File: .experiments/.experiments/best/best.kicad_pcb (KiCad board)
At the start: 2 copper layers, 140 x 90 mm, 39 parts, among them J1 USB_C, J2 Output, J3 Debug, Q1 FS8205A, U1 USBLC6-2SC6, U2 BQ24072, U3 HY2113-KB5B, U4 MT3608, U5 AP2112K-3.3, U6 LN61CN3302MR-G

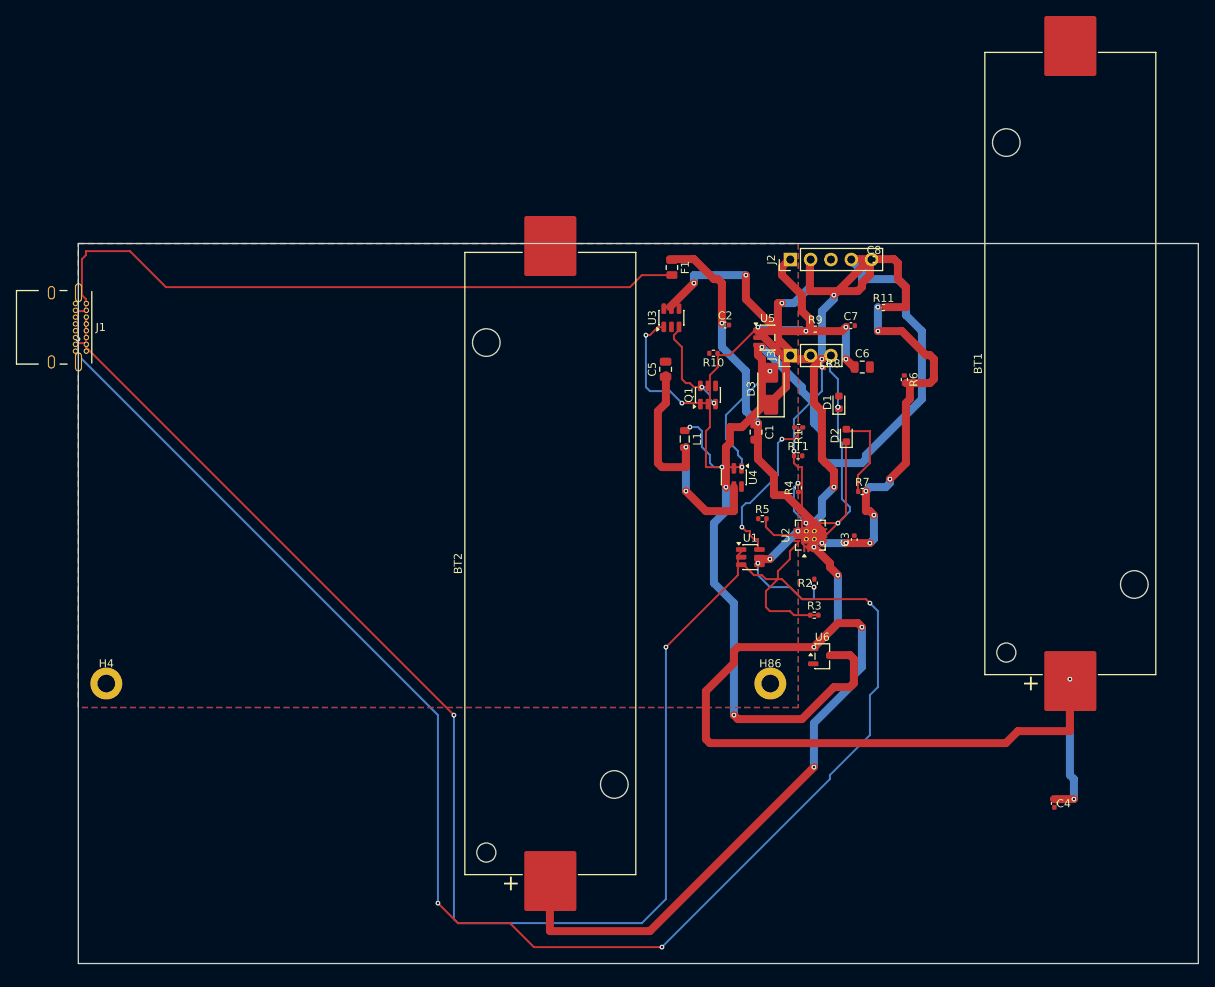
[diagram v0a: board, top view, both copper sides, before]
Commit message: Set uniform 6mil trace width (0.1524mm) for signal+power to reduce shorts
Baseline with 6mil: score=20.05 shorts=72 (vs 25.66@82shorts before)
Round 1: 20.45 shorts=93
Round 2: 20.65 shorts=84 [NEW BEST]
Round 3: 19.44 shorts=72

Trading off routing flexibility for cleaner DRC (no catastrophic shorts).
Tighter routing but more predictable.

Co-Authored-By: Claude Opus 4.6 <noreply@anthropic.com>
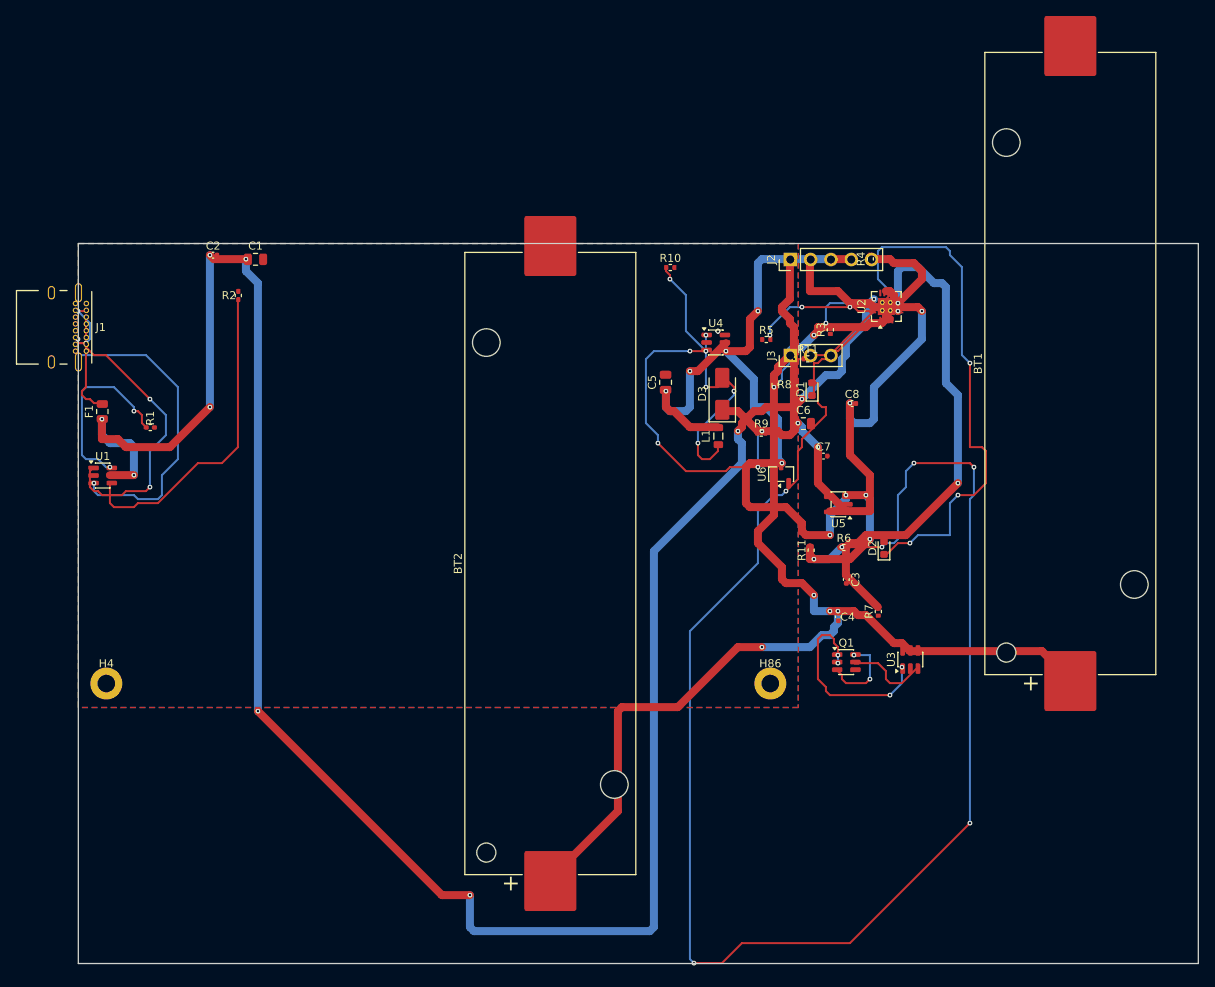
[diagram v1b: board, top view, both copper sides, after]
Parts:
- moved U1 81.6 mm to (3.04, 29.0)
- moved R1 81.0 mm to (9.00, 23.0), turned to 0 degrees
- moved R2 80.5 mm to (20.0, 6.50)
- moved F1 73.4 mm to (3.00, 21.0), turned to 90 degrees
- moved C1 66.2 mm to (22.1, 1.97), turned to 0 degrees
- moved C2 64.6 mm to (16.9, 1.46)
- moved U3 52.1 mm to (104.0, 52.0)
- moved Q1 37.6 mm to (96.0, 52.3), turned to 0 degrees
- moved R3 35.7 mm to (94.0, 10.8), turned to 90 degrees
- moved C4 35.7 mm to (95.0, 46.7)
- moved R11 31.7 mm to (91.6, 38.3), turned to 90 degrees
- moved U2 30.1 mm to (101.0, 7.87)
- moved R4 30.0 mm to (99.0, 1.92)
- moved U6 23.3 mm to (87.8, 28.8), turned to 90 degrees
- moved U5 22.6 mm to (95.0, 32.6), turned to 180 degrees
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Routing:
- net /VBUS: track 52.8 -> 269.7 mm, vias 4 -> 10
- net Net-(D1-A): track 0.00 -> 193.9 mm, vias 0 -> 6
- net Net-(J1-CC2): track 192.1 -> 40.6 mm, vias 4 -> 2
- net Net-(J1-CC1): track 169.9 -> 38.4 mm
- net /VBAT: track 253.3 -> 161.6 mm, vias 12 -> 6
- net Net-(F1-Pad2): track 89.4 -> 17.4 mm, vias 0 -> 2
- net /EN: track 146.3 -> 89.6 mm, vias 4 -> 8
- net Net-(D2-K): track 13.0 -> 67.3 mm, vias 0 -> 4
- net /3V3: track 26.4 -> 60.0 mm
- net Net-(R2-Pad1): track 11.2 -> 40.3 mm, vias 2 -> 0
- net /VSYS: track 51.9 -> 72.6 mm, vias 8 -> 6
- net Net-(U4-FB): track 31.3 -> 51.0 mm, vias 2 -> 6
- net Net-(D2-A): track 11.1 -> 0.00 mm
- net Net-(U2-TMR): track 5.41 -> 15.7 mm, vias 0 -> 2
- net /NTC_SENSE: track 27.0 -> 17.6 mm
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
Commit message: Hard-block cross-net traces to eliminate shorts (50% of DRC failures)
Critical fixes:
- Mark routed traces/vias at 1e6 (hard block) in solve() instead of 100 (soft)
- A* now cannot cross completed nets → no more shorting through existing traces
- Mark escape vias on grid immediately (was invisible, caused via collisions)
- Add clearance margin to via markings (0.5mm approach distance enforced)
- Raise max_search to 2M (hard blocks require longer detours)
- Wire max_search config through __init__ and all find_path calls

Test added: test_hard_block_prevents_cross_net_routing verifies blocked cells
are uncrossable, forcing detours instead.

Expected impact: DRC shorts should drop from ~80 to near-zero.

Co-Authored-By: Claude Opus 4.6 <noreply@anthropic.com>
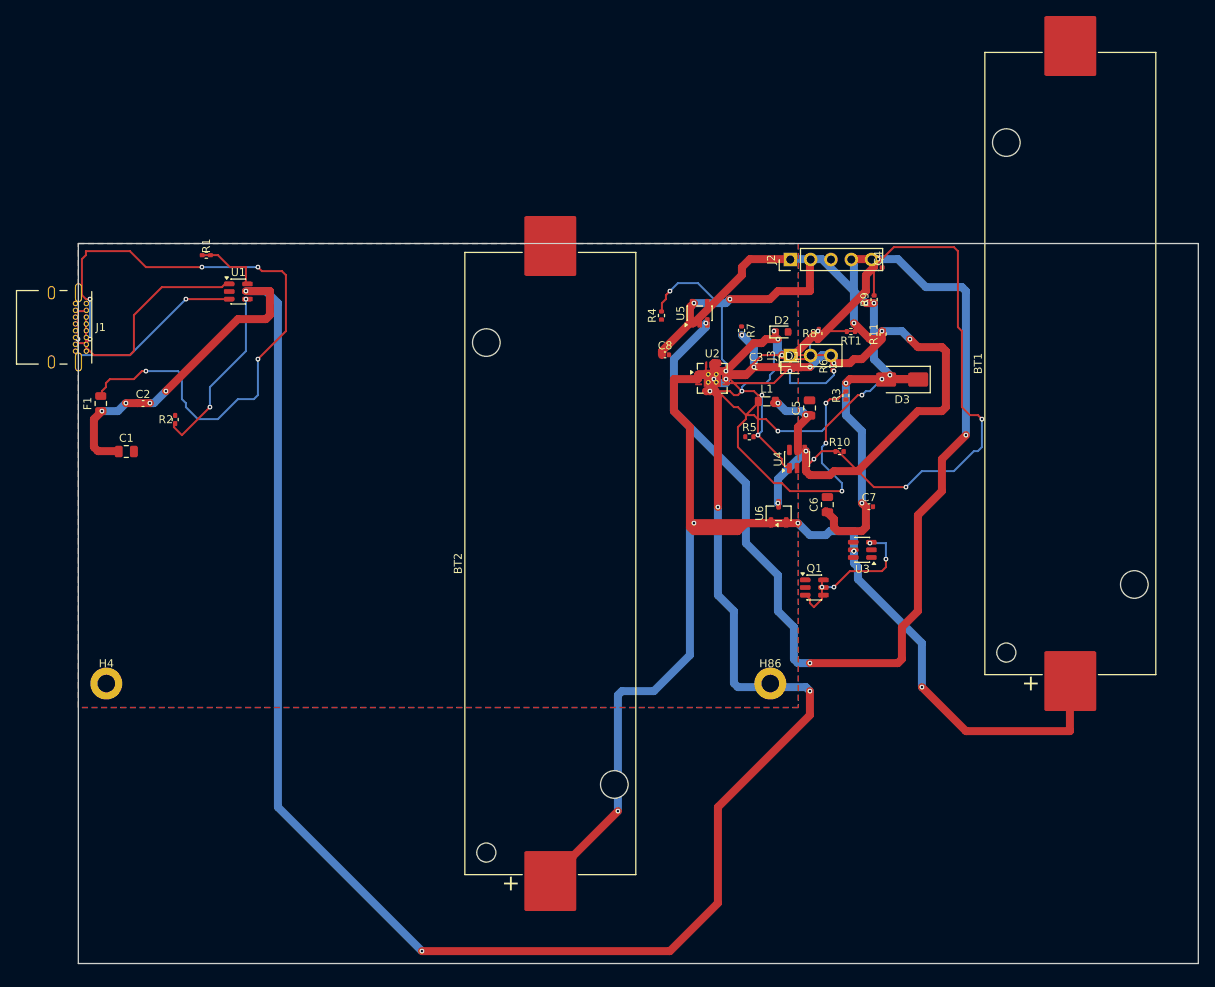
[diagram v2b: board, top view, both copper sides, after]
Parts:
- moved C4 44.0 mm to (100.0, 3.00), turned to 0 degrees
- moved R7 39.1 mm to (82.9, 10.9), turned to -90 degrees
- moved R10 31.3 mm to (95.2, 26.0)
- moved D2 29.9 mm to (87.9, 11.1), turned to 0 degrees
- moved U5 29.5 mm to (77.7, 8.72), turned to 90 degrees
- moved C1 28.9 mm to (6.00, 26.0)
- moved C3 28.9 mm to (84.7, 15.4), turned to 0 degrees
- moved U1 28.6 mm to (20.0, 6.00)
- moved R11 28.5 mm to (100.6, 11.3)
- moved R4 27.0 mm to (72.9, 9.00)
- moved C8 24.2 mm to (73.3, 13.9)
- moved U2 23.5 mm to (79.2, 16.8), turned to 0 degrees
- moved R6 22.7 mm to (94.3, 15.3), turned to 90 degrees
- moved R1 22.6 mm to (16.0, 1.47)
- moved D3 22.6 mm to (103.0, 17.0), turned to 180 degrees
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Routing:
- net Net-(D1-A): track 193.9 -> 9.12 mm, vias 6 -> 2
- net /EN: track 89.6 -> 190.2 mm, vias 8 -> 10
- net Net-(F1-Pad2): track 17.4 -> 88.4 mm, vias 2 -> 6
- net Net-(D2-K): track 67.3 -> 14.5 mm, vias 4 -> 2
- net /VSYS: track 72.6 -> 31.6 mm, vias 6 -> 7
- net /3V3: track 60.0 -> 27.3 mm
- net /VBAT: track 161.6 -> 192.1 mm, vias 6 -> 8
- net /5V: track 47.0 -> 77.3 mm, vias 2 -> 6
- net Net-(D3-A): track 25.6 -> 51.0 mm
- net Net-(Q1A-G): track 24.9 -> 0.00 mm, vias 4 -> 0
- net Net-(U2-ILIM): track 0.00 -> 19.3 mm, vias 0 -> 2
- net Net-(R2-Pad1): track 40.3 -> 22.2 mm, vias 0 -> 2
- net Net-(U4-FB): track 51.0 -> 68.3 mm, vias 6 -> 2
- net Net-(J1-CC2): track 40.6 -> 23.9 mm
- net Net-(U2-ISET): track 9.33 -> 26.0 mm
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
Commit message: Clean up: remove 50M+ of old experiment artifacts
Removed:
- .tmp_router_regression/ (11M baseline)
- .experiments/workers/ (40M+ old copies)
- .experiments/frames/ (old snapshots)

Kept: latest PCB, GIF, config, results

Co-Authored-By: Claude Opus 4.6 <noreply@anthropic.com>
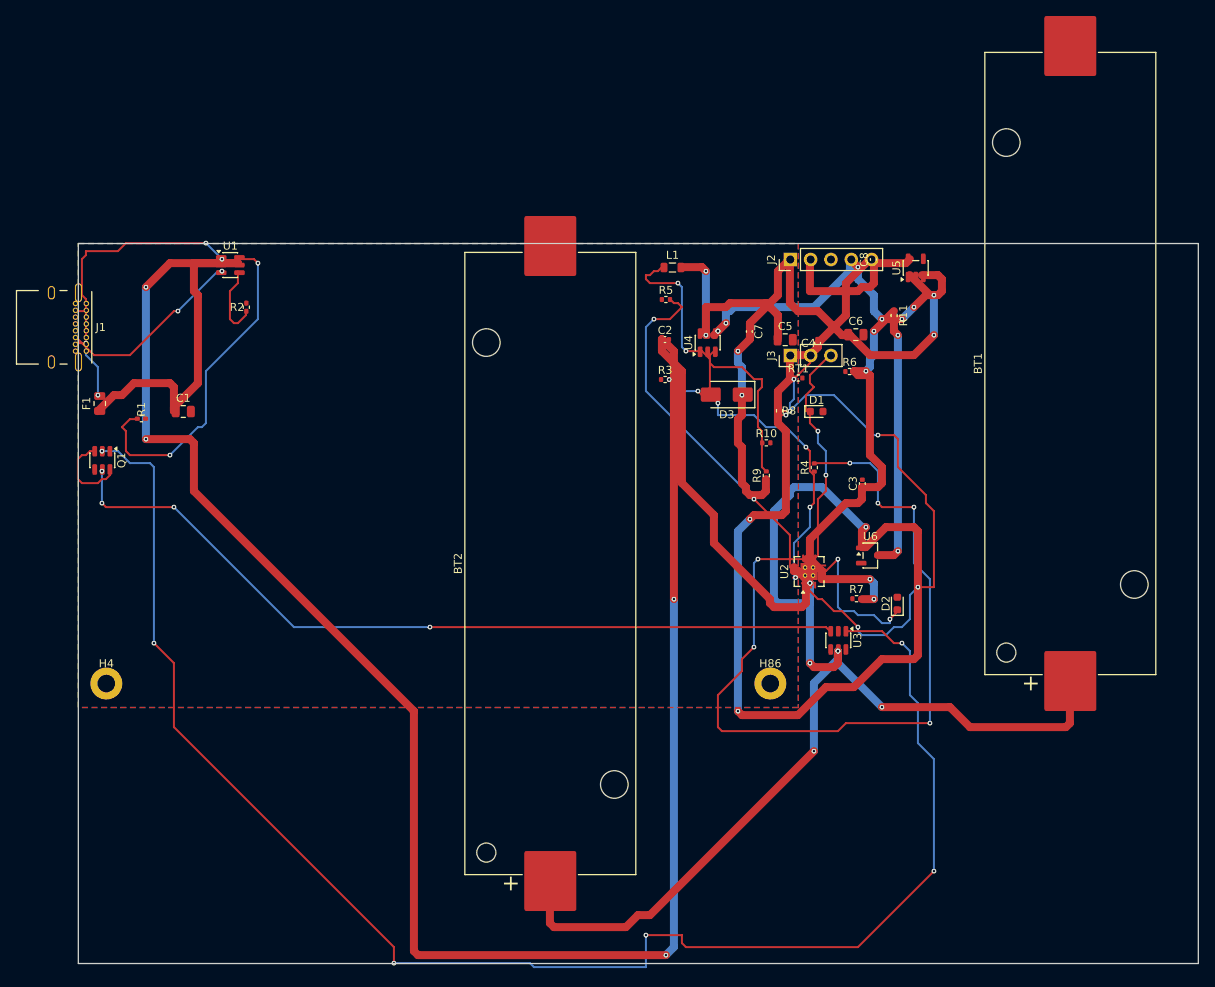
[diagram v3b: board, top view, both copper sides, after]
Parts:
- moved Q1 90.4 mm to (3.00, 27.1), turned to -90 degrees
- moved C2 65.7 mm to (73.3, 12.0)
- moved D2 36.9 mm to (102.4, 45.0), turned to 90 degrees
- moved R7 36.5 mm to (97.3, 44.4), turned to 0 degrees
- moved C8 28.6 mm to (99.4, 2.00), turned to 90 degrees
- moved U5 27.6 mm to (104.7, 3.04)
- moved U2 27.0 mm to (91.3, 41.0), turned to 90 degrees
- moved R4 26.9 mm to (92.0, 28.0)
- moved C7 26.5 mm to (83.9, 11.0), turned to -90 degrees
- moved R9 25.8 mm to (86.0, 29.0)
- moved R3 22.7 mm to (73.4, 17.0), turned to 0 degrees
- moved D3 22.0 mm to (81.1, 18.9)
- moved R1 22.0 mm to (7.89, 21.9)
- moved C6 21.5 mm to (97.2, 11.4), turned to 0 degrees
- moved L1 20.5 mm to (74.3, 3.00)
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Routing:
- net Net-(Q1A-G): track 0.00 -> 196.4 mm, vias 0 -> 6
- net /EN: track 190.2 -> 76.9 mm, vias 10 -> 8
- net Net-(Q1B-G): track 14.0 -> 101.6 mm
- net Net-(U2-ILIM): track 19.3 -> 100.6 mm, vias 2 -> 6
- net /VBAT: track 192.1 -> 270.3 mm, vias 8 -> 10
- net Net-(F1-Pad2): track 88.4 -> 13.1 mm, vias 6 -> 2
- net /VBUS: track 255.4 -> 311.1 mm, vias 8 -> 4
- net /NTC_SENSE: track 22.7 -> 72.1 mm, vias 2 -> 6
- net Net-(U4-FB): track 68.3 -> 21.2 mm, vias 2 -> 0
- net Net-(R1-Pad1): track 8.12 -> 42.9 mm, vias 0 -> 2
- net Net-(U2-TMR): track 13.4 -> 45.6 mm
- net Net-(D3-A): track 51.0 -> 24.4 mm, vias 4 -> 2
- net /VSYS: track 31.6 -> 55.9 mm, vias 7 -> 6
- net /VSYS_BOOST: track 10.2 -> 27.5 mm
- net /CHG_N: track 14.7 -> 29.1 mm, vias 1 -> 2
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
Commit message: Run 75-round experiment with 5mil traces: score 29.0
Configured all traces (signal and power) to 5 mil (0.127mm).
Best layout: 26/26 nets routed, 531 traces, 92 vias, 2487mm total length.
DRC: 242 violations (improved from 339 baseline).

Best config: clearance=0.1757mm, edge_margin=5.8486mm, cooling_factor=0.9698

Co-Authored-By: Claude Opus 4.6 <noreply@anthropic.com>
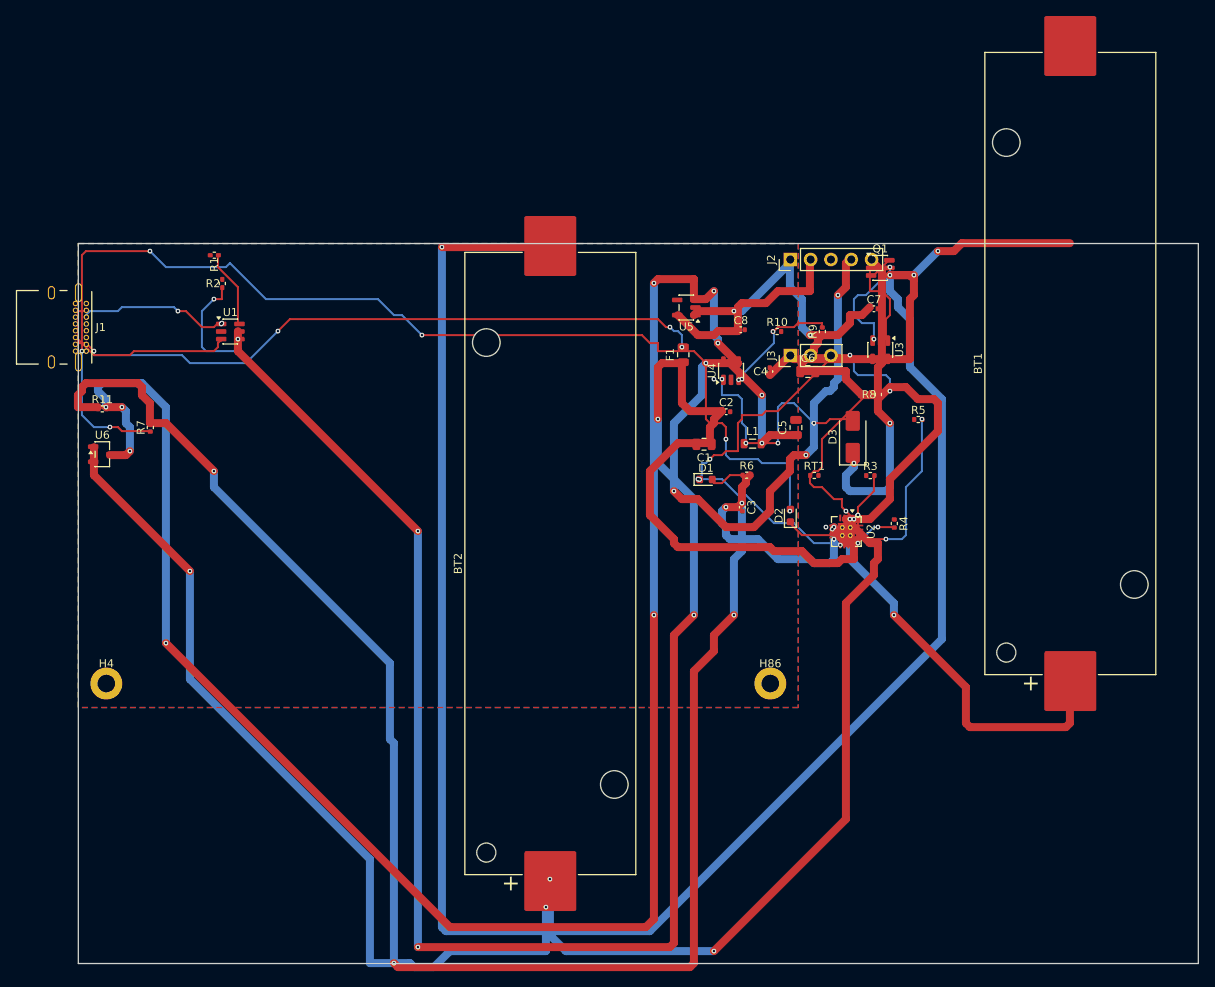
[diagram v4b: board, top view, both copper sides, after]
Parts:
- moved Q1 100.2 mm to (100.2, 3.04), turned to 0 degrees
- moved R11 99.7 mm to (3.00, 20.7), turned to 0 degrees
- moved U6 96.8 mm to (3.00, 26.3)
- moved R7 90.8 mm to (9.00, 23.0), turned to 90 degrees
- moved F1 73.2 mm to (75.6, 13.9)
- moved C1 65.2 mm to (78.2, 25.1), turned to 180 degrees
- moved U3 36.7 mm to (100.2, 13.3)
- moved R5 34.9 mm to (105.0, 22.0)
- moved U5 29.1 mm to (76.0, 8.00), turned to 180 degrees
- moved R3 28.3 mm to (99.0, 29.0)
- moved L1 24.2 mm to (84.3, 25.0)
- moved R1 22.4 mm to (17.0, 1.47), turned to 180 degrees
- moved R9 19.3 mm to (93.0, 11.0)
- moved C8 18.7 mm to (82.8, 10.8), turned to 0 degrees
- moved R6 18.3 mm to (83.5, 29.0)
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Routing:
- net /CELL_NEG: track 0.00 -> 265.1 mm, vias 0 -> 4
- net /EN: track 76.9 -> 302.6 mm, vias 8 -> 12
- net Net-(Q1A-G): track 196.4 -> 11.1 mm, vias 6 -> 0
- net /VSYS: track 55.9 -> 229.6 mm, vias 6 -> 7
- net Net-(D2-A): track 0.00 -> 142.2 mm, vias 0 -> 6
- net Net-(U2-ILIM): track 100.6 -> 5.83 mm, vias 6 -> 3
- net Net-(Q1B-G): track 101.6 -> 13.4 mm, vias 4 -> 2
- net Net-(F1-Pad2): track 13.1 -> 86.4 mm, vias 2 -> 4
- net /VBUS: track 311.1 -> 257.3 mm
- net /VBAT: track 270.3 -> 318.1 mm, vias 10 -> 7
- net Net-(R1-Pad1): track 42.9 -> 9.54 mm, vias 2 -> 0
- net /NTC_SENSE: track 72.1 -> 39.0 mm, vias 6 -> 2
- net Net-(U2-ISET): track 39.3 -> 7.33 mm, vias 6 -> 0
- net Net-(U2-TMR): track 45.6 -> 21.7 mm
- net /CHG_N: track 29.1 -> 47.7 mm, vias 2 -> 5
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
